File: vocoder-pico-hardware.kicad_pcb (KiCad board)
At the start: 2 copper layers, 47 x 108 mm, 68 parts, among them J1 Conn_02x05_Odd_Even, J2 AudioJack2_SwitchT, J3 AudioJack2_SwitchT, Q1 BC547, Q2 BC547, Q3 BC547, Q4 BC547, SW1 SW_Push, SW2 SW_Push, U1 TL072, U2 LM7805_TO220, U3 PCM5100A, U4 SC39-11GWA, U5 SC39-11GWA, U6 SC39-11GWA, U7 SC39-11GWA, U8 MCP6002-xP

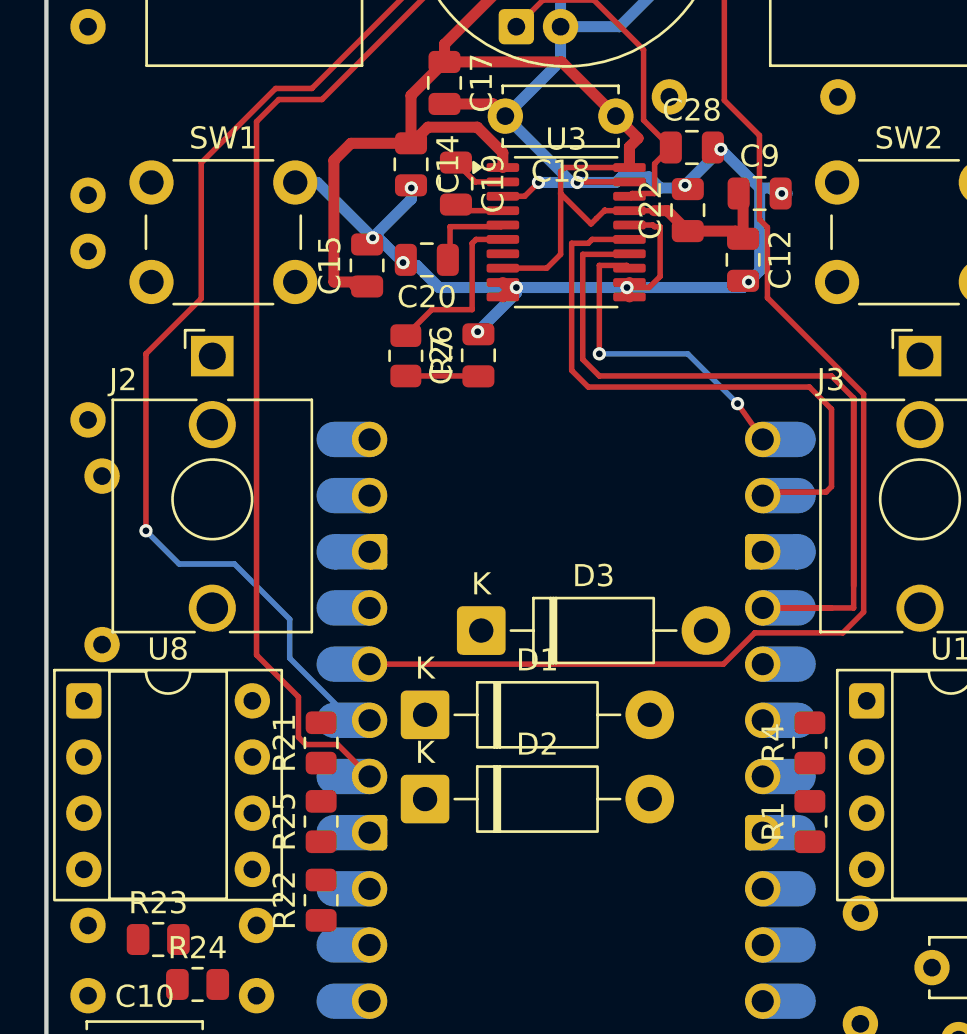
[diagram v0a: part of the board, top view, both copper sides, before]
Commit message: finish routing of i2s section for inmp441
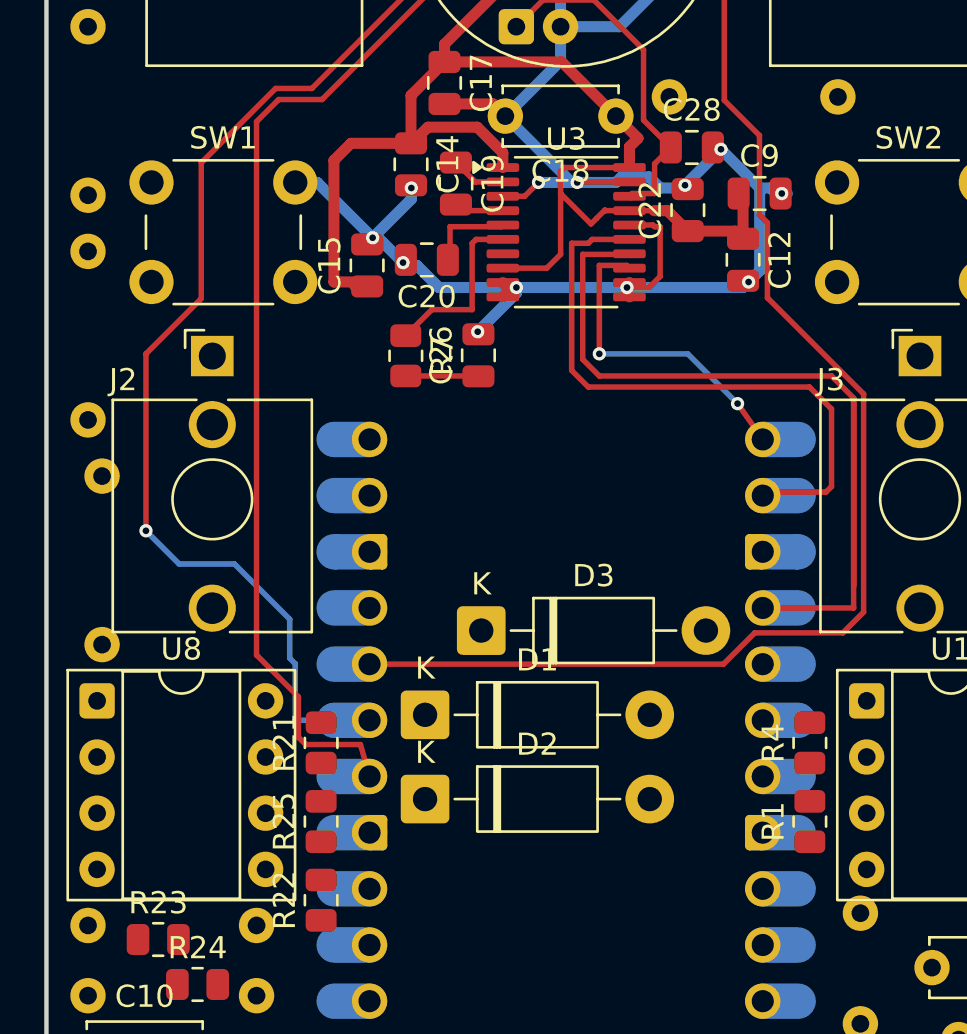
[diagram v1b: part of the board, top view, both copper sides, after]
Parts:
- moved U8 0.60 mm to (56.3, 99.2)
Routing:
- net Net-(A1-GPIO18): track 45.1 -> 41.9 mm
- net Net-(A1-GPIO11): track 49.0 -> 51.3 mm

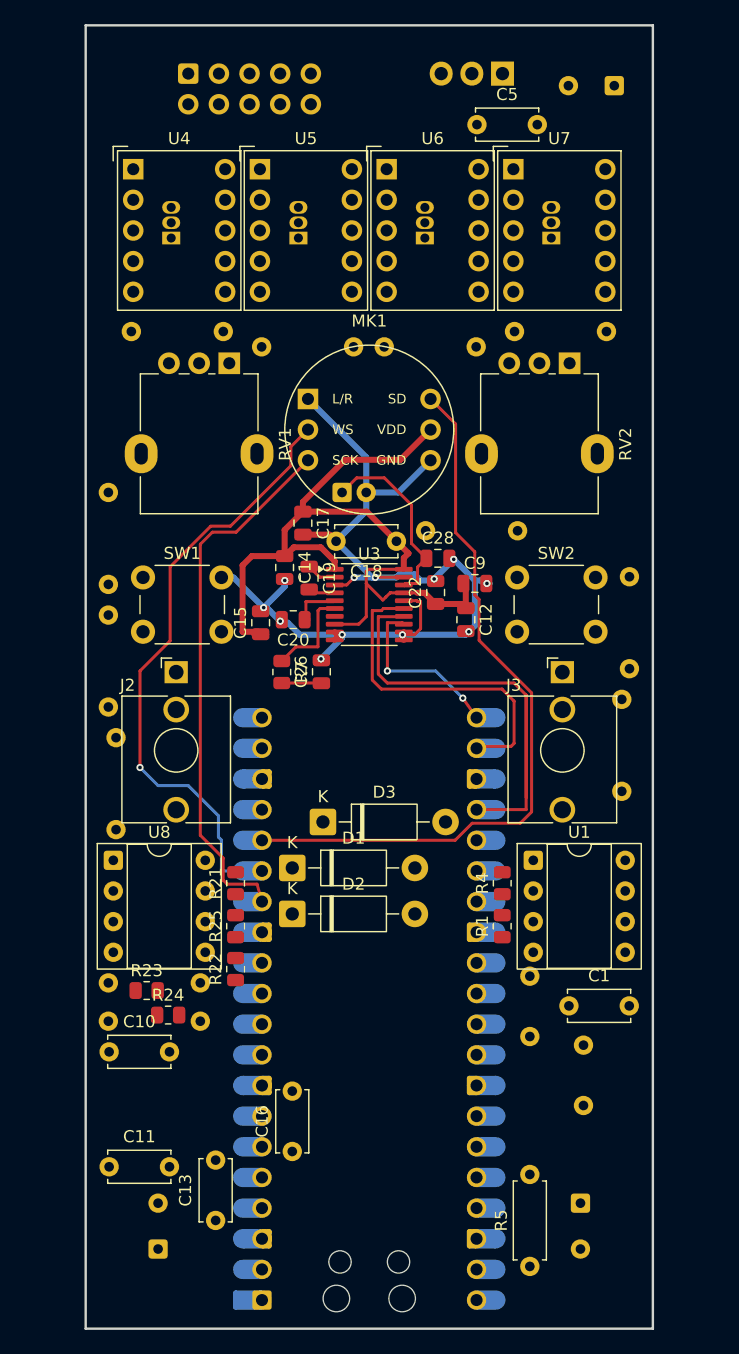
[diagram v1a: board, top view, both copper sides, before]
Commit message: put the width to 12TE
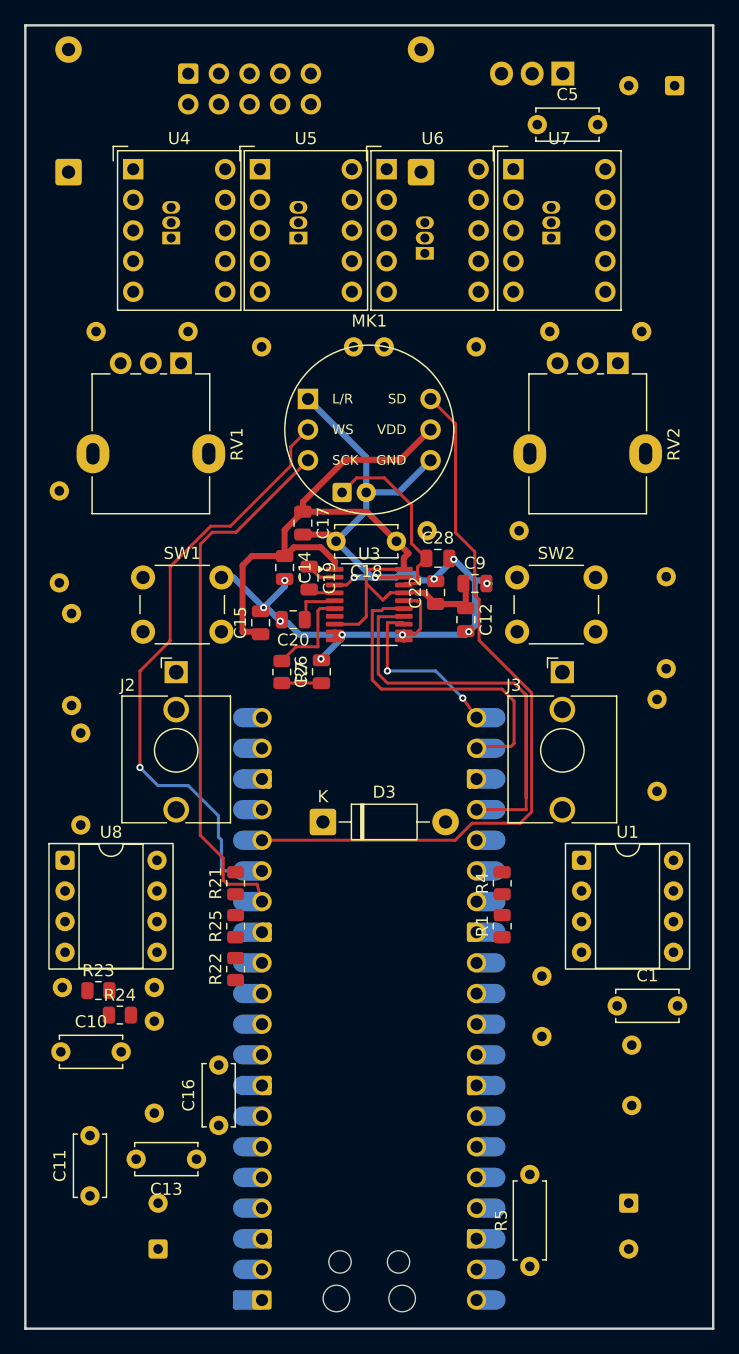
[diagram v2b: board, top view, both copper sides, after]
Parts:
- D1, D2: moved to B.Cu
- moved D2 64.2 mm to (52.6, 42.2), turned to 90 degrees
- moved D1 58.6 mm to (81.8, 42.2), turned to 90 degrees
- moved R16 8.52 mm to (59.7, 120.1), turned to 90 degrees
- moved C16 6.47 mm to (65.0, 121.2)
- moved C13 5.32 mm to (63.2, 124.0), turned to 180 degrees
- moved C6 5.00 mm to (102.8, 35.0)
- moved C5 5.00 mm to (91.4, 38.2)
- moved U2 5.00 mm to (93.5, 34.0)
- moved R10 4.07 mm to (51.8, 76.2)
- moved RV1 4.00 mm to (61.9, 58.0)
- moved C1 4.00 mm to (98.0, 111.3)
- moved C10 4.00 mm to (51.9, 115.1)
- moved C3 4.00 mm to (99.0, 127.6)
- moved C7 4.00 mm to (99.2, 119.5)
- moved R23 4.00 mm to (55.1, 110.0)
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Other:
- board size 47 x 108 mm -> 57 x 108 mm

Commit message: make polarized capacitators consistent
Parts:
- C3, C4, C6: footprint Capacitor_THT:CP_Radial_D8.0mm_P3.80mm -> Capacitor_THT:CP_Radial_D5.0mm_P2.00mm
- moved C4 97.7 mm to (99.8, 42.2), turned to 0 degrees
- moved C3 93.5 mm to (51.6, 47.0), turned to 0 degrees
- moved C6 2.98 mm to (99.8, 35.1), turned to 0 degrees

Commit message: begin power supply routing
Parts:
- moved D2 10.2 mm to (52.5, 32.0), turned to -90 degrees
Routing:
- net -12V: track 0.00 -> 97.8 mm
- net +12V: track 0.00 -> 15.1 mm
- net Net-(D2-K): track 0.00 -> 13.4 mm
- net Net-(D1-A): track 0.00 -> 12.5 mm

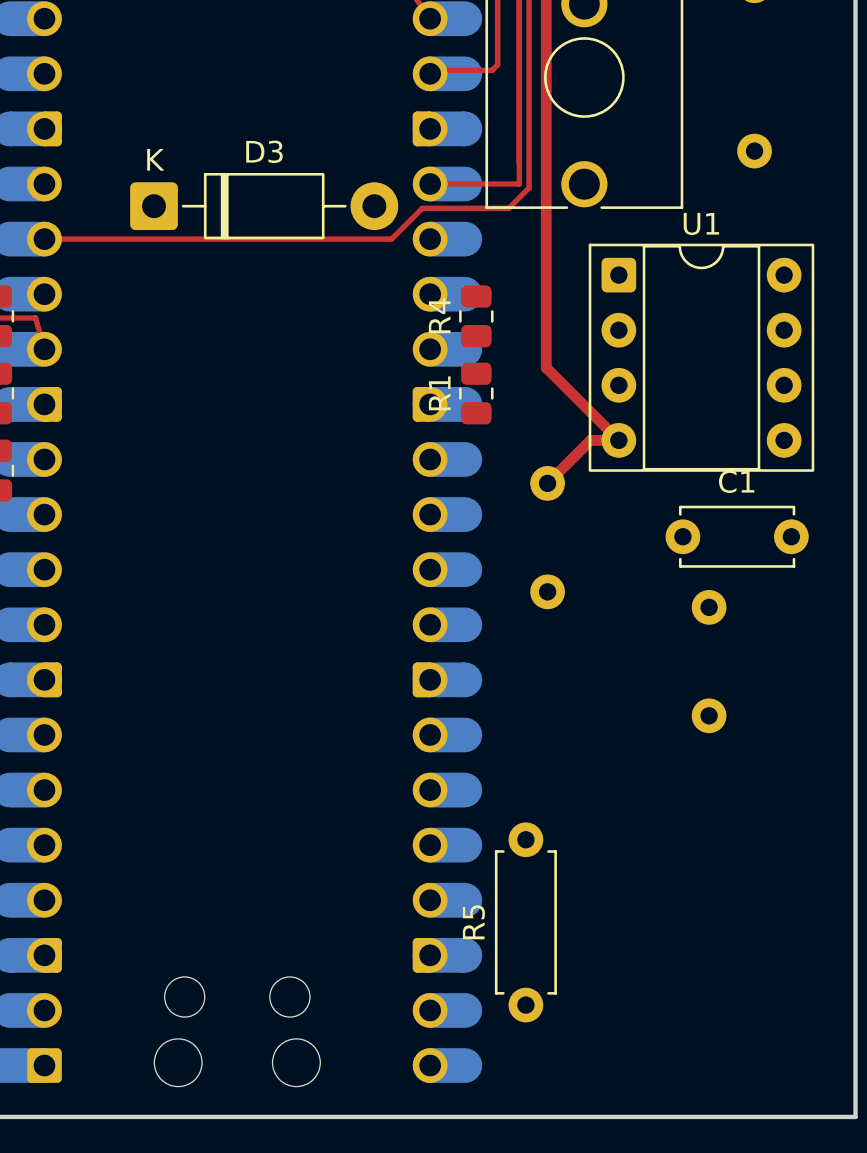
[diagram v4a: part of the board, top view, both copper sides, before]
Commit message: continue power supply routing / relocate D3
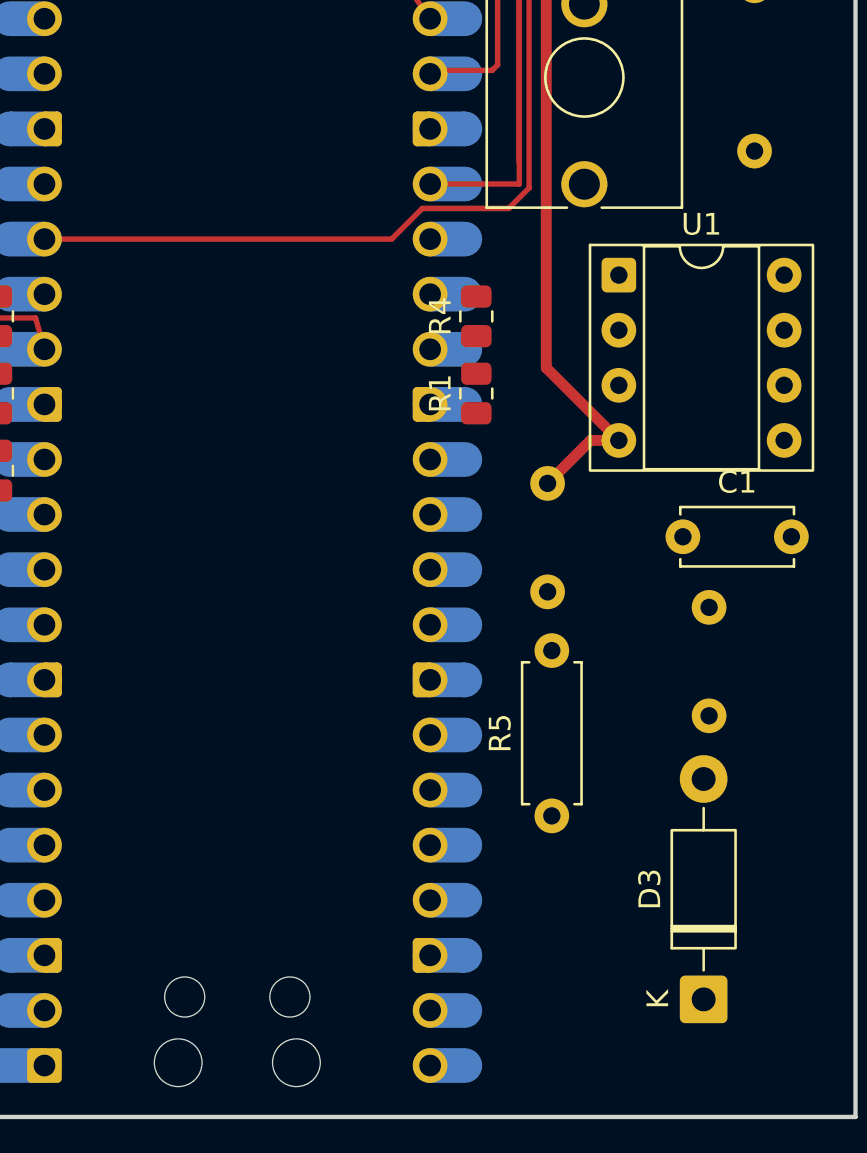
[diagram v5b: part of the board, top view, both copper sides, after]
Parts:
- moved D3 44.5 mm to (99.0, 132.6), turned to 90 degrees
- moved R5 8.80 mm to (92.0, 124.1)
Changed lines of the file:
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@@
 	(footprint "Resistor_THT:R_Axial_DIN0207_L6.3mm_D2.5mm_P7.62mm_Horizontal"
 		(layer "F.Cu")
-		(at 90.805 132.842 90)
+		(at 92 124.12 90)
 		(descr "Resistor, Axial_DIN0207 series, Axial, Horizontal, pin pitch=7.62mm, 0.25W = 1/4W, length*diameter=6.3*2.5mm^2, http://cdn-reichelt.de/documents/datenblatt/B400/1_4W%23YAG.pdf")
 		(tags "Resistor Axial_DIN0207 series Axial Horizontal pin pitch 7.62mm 0.25W = 1/4W length 6.3mm diameter 2.5mm")
@@
 	(footprint "Diode_THT:D_DO-41_SOD81_P10.16mm_Horizontal"
 		(layer "F.Cu")
-		(at 73.66 96.012)
+		(at 99 132.58 90)
 		(descr "Diode, DO-41_SOD81 series, Axial, Horizontal, pin pitch=10.16mm, length*diameter=5.2*2.7mm^2, https://www.diodes.com/assets/Package-Files/DO-41-Plastic.pdf")
 		(tags "Diode DO-41_SOD81 series Axial Horizontal pin pitch 10.16mm  length 5.2mm diameter 2.7mm")
 		(property "Reference" "D3"
-			(at 5.08 -2.47 0)
+			(at 5.08 -2.47 90)
 			(layer "F.SilkS")
 			(effects
@@
 		)
 		(property "Value" "1N5817"
-			(at 5.08 2.47 0)
+			(at 5.08 2.47 90)
 			(layer "F.Fab")
 			(effects
@@
 		)
 		(property "Datasheet" "http://www.vishay.com/docs/88525/1n5817.pdf"
-			(at 0 0 0)
+			(at 0 0 90)
 			(layer "F.Fab")
 			(hide yes)
@@
 		)
 		(property "Description" "20V 1A Schottky Barrier Rectifier Diode, DO-41"
-			(at 0 0 0)
+			(at 0 0 90)
 			(layer "F.Fab")
 			(hide yes)
@@
 		(attr through_hole)
 		(fp_line
+			(start 3.38 -1.47)
+			(end 3.38 1.47)
+			(stroke
+				(width 0.12)
+				(type solid)
+			)
+			(layer "F.SilkS")
+		)
+		(fp_line
+			(start 3.26 -1.47)
+			(end 3.26 1.47)
+			(stroke
+				(width 0.12)
+				(type solid)
+			)
+			(layer "F.SilkS")
+		)
+		(fp_line
+			(start 3.14 -1.47)
+			(end 3.14 1.47)
+			(stroke
+				(width 0.12)
+				(type solid)
+			)
+			(layer "F.SilkS")
+		)
+		(fp_line
+			(start 8.82 0)
+			(end 7.8 0)
+			(stroke
+				(width 0.12)
+				(type solid)
+			)
+			(layer "F.SilkS")
+		)
+		(fp_line
 			(start 1.34 0)
 			(end 2.36 0)
@@
 			(layer "F.SilkS")
 		)
-		(fp_line
-			(start 3.14 -1.47)
-			(end 3.14 1.47)
-			(stroke
-				(width 0.12)
-				(type solid)
-			)
-			(layer "F.SilkS")
-		)
-		(fp_line
-			(start 3.26 -1.47)
-			(end 3.26 1.47)
-			(stroke
-				(width 0.12)
-				(type solid)
-			)
-			(layer "F.SilkS")
-		)
-		(fp_line
-			(start 3.38 -1.47)
-			(end 3.38 1.47)
-			(stroke
-				(width 0.12)
-				(type solid)
-			)
-			(layer "F.SilkS")
-		)
-		(fp_line
-			(start 8.82 0)
-			(end 7.8 0)
-			(stroke
-				(width 0.12)
-				(type solid)
-			)
-			(layer "F.SilkS")
-		)
 		(fp_rect
 			(start 2.36 -1.47)
@@
 		)
 		(fp_line
+			(start 3.36 -1.35)
+			(end 3.36 1.35)
+			(stroke
+				(width 0.1)
+				(type solid)
+			)
+			(layer "F.Fab")
+		)
+		(fp_line
+			(start 3.26 -1.35)
+			(end 3.26 1.35)
+			(stroke
+				(width 0.1)
+				(type solid)
+			)
+			(layer "F.Fab")
+		)
+		(fp_line
+			(start 3.16 -1.35)
+			(end 3.16 1.35)
+			(stroke
+				(width 0.1)
+				(type solid)
+			)
+			(layer "F.Fab")
+		)
+		(fp_line
+			(start 10.16 0)
+			(end 7.68 0)
+			(stroke
+				(width 0.1)
+				(type solid)
+			)
+			(layer "F.Fab")
+		)
+		(fp_line
 			(start 0 0)
 			(end 2.48 0)
@@
 			(layer "F.Fab")
 		)
-		(fp_line
-			(start 3.16 -1.35)
-			(end 3.16 1.35)
-			(stroke
-				(width 0.1)
-				(type solid)
-			)
-			(layer "F.Fab")
-		)
-		(fp_line
-			(start 3.26 -1.35)
-			(end 3.26 1.35)
-			(stroke
-				(width 0.1)
-				(type solid)
-			)
-			(layer "F.Fab")
-		)
-		(fp_line
-			(start 3.36 -1.35)
-			(end 3.36 1.35)
-			(stroke
-				(width 0.1)
-				(type solid)
-			)
-			(layer "F.Fab")
-		)
-		(fp_line
-			(start 10.16 0)
-			(end 7.68 0)
-			(stroke
-				(width 0.1)
-				(type solid)
-			)
-			(layer "F.Fab")
-		)
 		(fp_rect
 			(start 2.48 -1.35)
@@
 		)
 		(fp_text user "K"
-			(at 0 -2.1 0)
+			(at 0 -2.1 90)
 			(layer "F.SilkS")
 			(effects
@@
 		)
 		(fp_text user "K"
-			(at 0 -2.1 0)
+			(at 0 -2.1 90)
 			(layer "F.Fab")
 			(effects
@@
 		)
 		(fp_text user "${REFERENCE}"
-			(at 5.47 0 0)
+			(at 5.47 0 90)
 			(layer "F.Fab")
 			(effects
@@
 		)
 		(pad "1" thru_hole roundrect
-			(at 0 0)
+			(at 0 0 90)
 			(size 2.2 2.2)
 			(drill 1.1)
@@
 		)
 		(pad "2" thru_hole circle
-			(at 10.16 0)
+			(at 10.16 0 90)
 			(size 2.2 2.2)
 			(drill 1.1)
